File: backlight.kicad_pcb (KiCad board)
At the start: 2 copper layers, 29.3 x 19.6 mm, 18 parts, among them P1 CONN_01X05, U1 APA102C, U2 APA102C, U3 APA102C, U4 APA102C, U5 APA102C, U6 APA102C, U7 APA102C, U8 APA102C, U9 APA102C

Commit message: Modified pcb design
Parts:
- removed the REF** at (148.6, 68.5)
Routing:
- net GND: track 3.06 -> 1.16 mm
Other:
- board size 29.3 x 19.6 mm -> 27.8 x 19.6 mm
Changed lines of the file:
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@@
 (kicad_pcb (version 4) (host pcbnew 4.0.2-stable)
   (general
-    (links 42)
+    (links 41)
     (no_connects 0)
     (area 117.296429 53.075 155.703572 78.675)
     (thickness 1.6)
     (drawings 4)
-    (tracks 100)
+    (tracks 99)
     (zones 0)
-    (modules 18)
+    (modules 17)
     (nets 22)
   )
@@
   )
   (setup
-    (last_trace_width 0.3)
+    (last_trace_width 0.25)
     (user_trace_width 0.3)
     (user_trace_width 0.5)
@@
     (trace_min 0.2)
     (segment_width 0.2)
-    (edge_width 0.15)
+    (edge_width 0.05)
     (via_size 0.6)
     (via_drill 0.4)
@@
     (mod_text_size 1 1)
     (mod_text_width 0.15)
-    (pad_size 1.5 1.5)
-    (pad_drill 1.5)
+    (pad_size 1.3 2)
+    (pad_drill 0)
     (pad_to_mask_clearance 0.2)
     (aux_axis_origin 154 55.6)
@@
     (visible_elements 7FFFFF7F)
     (pcbplotparams
-      (layerselection 0x00000_80000001)
+      (layerselection 0x01008_80000001)
       (usegerberextensions false)
       (excludeedgelayer true)
@@
       (psnegative false)
       (psa4output false)
-      (plotreference true)
-      (plotvalue true)
+      (plotreference false)
+      (plotvalue false)
       (plotinvisibletext false)
       (padsonsilk false)
@@
     (fp_line (start 6.8 4.8) (end 6.8 -4.1) (layer F.CrtYd) (width 0.05))
     (fp_line (start 6.8 -4.1) (end -6.8 -4.1) (layer F.CrtYd) (width 0.05))
-    (pad 1 smd rect (at -2.5 -2.44 90) (size 0.8 1.9) (layers F.Cu F.Paste F.Mask)
+    (pad 1 thru_hole rect (at -2.5 -2.44 90) (size 0.8 1.9) (drill 0.5) (layers *.Cu *.Mask F.SilkS)
       (net 1 GND))
     (pad 2 smd rect (at -1.25 -2.44 90) (size 0.8 1.9) (layers F.Cu F.Paste F.Mask)
@@
     (pad 5 smd rect (at 2.5 -2.44 90) (size 0.8 1.9) (layers F.Cu F.Paste F.Mask)
       (net 20 /MOSI))
-    (pad "" smd rect (at 5.35 2.44 90) (size 1.3 3.35) (layers F.Cu F.Paste F.Mask))
-    (pad "" smd rect (at -5.35 2.44 90) (size 1.3 3.35) (layers F.Cu F.Paste F.Mask))
+    (pad "" smd rect (at 5.35 1.56 90) (size 1.3 2) (layers F.Cu F.Paste F.Mask))
+    (pad "" smd rect (at -5.35 1.56 90) (size 1.3 2) (layers F.Cu F.Paste F.Mask))
     (model Connectors_Molex.3dshapes/Molex_Panelmate-53780-0570_05x1.25mm_Angled.wrl
       (at (xyz 0 0 0))
@@
       (rotate (xyz 0 0 0))
     )
-  )
-  (module backlight:1pin (layer F.Cu)
-    (at 148.6 68.5)
-    (descr "module 1 pin (ou trou mecanique de percage)")
-    (tags DEV)
-    (fp_text reference REF** (at 0 -3.048) (layer F.SilkS) hide
-      (effects (font (size 1 1) (thickness 0.15)))
-    )
-    (fp_text value 1pin (at 0 2.794) (layer F.Fab) hide
-      (effects (font (size 1 1) (thickness 0.15)))
-    )
-    (pad 1 thru_hole circle (at 0 0) (size 1 1) (drill 0.4) (layers *.Cu *.Mask F.SilkS)
-      (net 1 GND))
   )
   (module backlight:TantalC_SizeR_EIA-2012 (layer F.Cu)
@@
     )
   )
-  (gr_line (start 153.3 75.8) (end 153.3 56.2) (layer Edge.Cuts) (width 0.15))
-  (gr_line (start 124 75.8) (end 153.3 75.8) (layer Edge.Cuts) (width 0.15))
-  (gr_line (start 124 56.2) (end 124 75.8) (layer Edge.Cuts) (width 0.15))
-  (gr_line (start 153.3 56.2) (end 124 56.2) (layer Edge.Cuts) (width 0.15))
+  (gr_line (start 151.8 75.8) (end 151.8 56.2) (layer Edge.Cuts) (width 0.05))
+  (gr_line (start 124 75.8) (end 151.8 75.8) (layer Edge.Cuts) (width 0.05))
+  (gr_line (start 124 56.2) (end 124 75.8) (layer Edge.Cuts) (width 0.05))
+  (gr_line (start 151.8 56.2) (end 124 56.2) (layer Edge.Cuts) (width 0.05))
   (segment (start 146.55 69.6) (end 146.55 68.65) (width 0.5) (layer F.Cu) (net 1))
   (segment (start 146.55 68.65) (end 146.7 68.5) (width 0.5) (layer F.Cu) (net 1))
-  (segment (start 146.7 68.5) (end 148.6 68.5) (width 0.8) (layer F.Cu) (net 1))
   (segment (start 137.6 60.75) (end 139 60.75) (width 1) (layer F.Cu) (net 2))
   (segment (start 137.6 62.25) (end 139 62.25) (width 1) (layer F.Cu) (net 3))

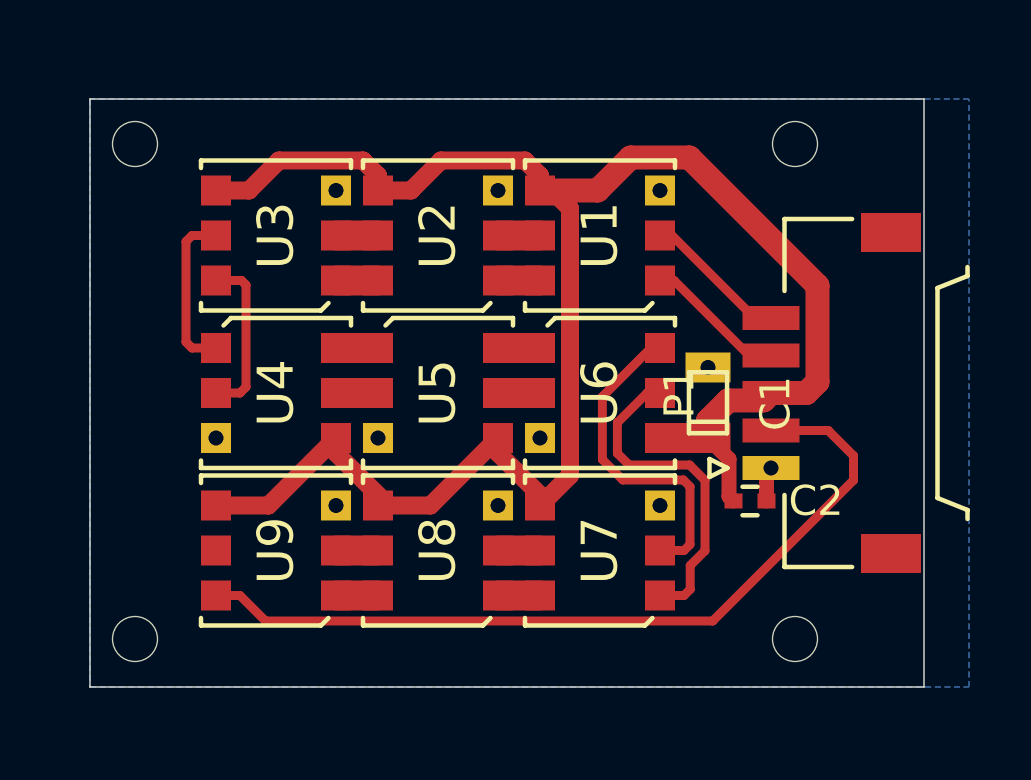
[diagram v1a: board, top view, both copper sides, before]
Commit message: Avoid long staight trace
To make it more auto level friendly
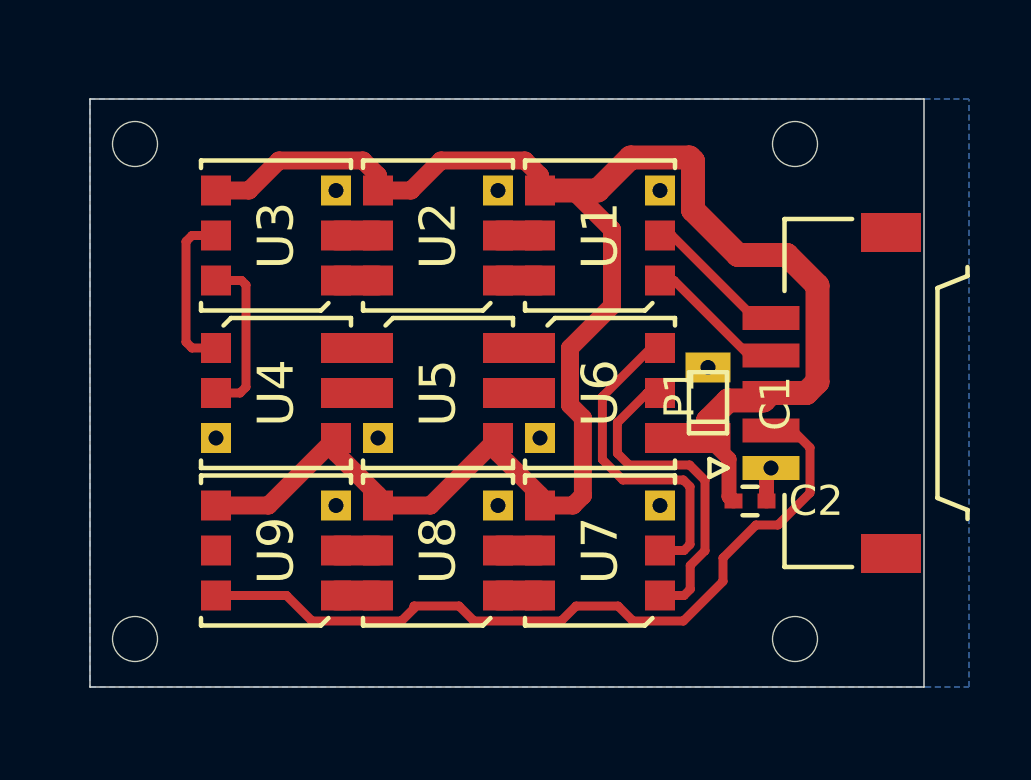
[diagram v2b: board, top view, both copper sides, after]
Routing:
- net VCC: track 63.9 -> 67.8 mm
- net /MISO: track 27.5 -> 26.3 mm
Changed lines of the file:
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@@
     (thickness 1.6)
     (drawings 4)
-    (tracks 99)
+    (tracks 122)
     (zones 0)
     (modules 17)
@@
   )
   (setup
-    (last_trace_width 0.25)
+    (last_trace_width 0.3)
     (user_trace_width 0.3)
     (user_trace_width 0.5)
@@
     (pad_drill 0)
     (pad_to_mask_clearance 0.2)
-    (aux_axis_origin 154 55.6)
-    (grid_origin 154 55.6)
+    (aux_axis_origin 152 55.9)
+    (grid_origin 152 55.9)
     (visible_elements 7FFFFF7F)
     (pcbplotparams
@@
   (segment (start 137.6 71.25) (end 139 71.25) (width 1) (layer F.Cu) (net 12))
   (segment (start 137.6 72.75) (end 139 72.75) (width 1) (layer F.Cu) (net 13))
-  (segment (start 139 69.75) (end 140.000001 68.749999) (width 0.6) (layer F.Cu) (net 14))
-  (segment (start 140.000001 68.749999) (end 140.000001 59.849999) (width 0.6) (layer F.Cu) (net 14))
-  (segment (start 140.000001 59.849999) (end 139.400002 59.25) (width 0.6) (layer F.Cu) (net 14))
+  (segment (start 145.6 61.4) (end 147.230002 61.4) (width 0.8) (layer F.Cu) (net 14))
+  (segment (start 147.230002 61.4) (end 148.250001 62.419999) (width 0.8) (layer F.Cu) (net 14))
+  (segment (start 144.100001 59.900001) (end 145.6 61.4) (width 0.8) (layer F.Cu) (net 14))
+  (segment (start 143.980001 58.149999) (end 144.100001 58.269999) (width 0.8) (layer F.Cu) (net 14))
+  (segment (start 144.100001 58.269999) (end 144.100001 59.900001) (width 0.8) (layer F.Cu) (net 14))
+  (segment (start 140.000001 66.400001) (end 140.42998 66.82998) (width 0.6) (layer F.Cu) (net 14))
+  (segment (start 140.42998 66.82998) (end 140.42998 69.42002) (width 0.6) (layer F.Cu) (net 14))
+  (segment (start 140.42998 69.42002) (end 140.1 69.75) (width 0.6) (layer F.Cu) (net 14))
+  (segment (start 140.1 69.75) (end 139 69.75) (width 0.6) (layer F.Cu) (net 14))
+  (segment (start 141.4 63.1) (end 140.000001 64.499999) (width 0.6) (layer F.Cu) (net 14))
+  (segment (start 140.000001 64.499999) (end 140.000001 66.400001) (width 0.6) (layer F.Cu) (net 14))
+  (segment (start 141.4 60.55) (end 141.4 63.1) (width 0.6) (layer F.Cu) (net 14))
+  (segment (start 139 59.25) (end 140.1 59.25) (width 0.6) (layer F.Cu) (net 14))
+  (segment (start 140.1 59.25) (end 141.4 60.55) (width 0.6) (layer F.Cu) (net 14))
   (segment (start 139.400002 59.25) (end 139 59.25) (width 0.6) (layer F.Cu) (net 14))
   (segment (start 139 59.25) (end 140.919998 59.25) (width 0.8) (layer F.Cu) (net 14))
@@
   (segment (start 142.019999 58.149999) (end 143.980001 58.149999) (width 0.8) (layer F.Cu) (net 14))
   (segment (start 148.250001 65.630001) (end 147.880002 66) (width 0.8) (layer F.Cu) (net 14))
-  (segment (start 143.980001 58.149999) (end 148.250001 62.419999) (width 0.8) (layer F.Cu) (net 14))
   (segment (start 148.250001 62.419999) (end 148.250001 65.630001) (width 0.8) (layer F.Cu) (net 14))
   (segment (start 147.880002 66) (end 146.7 66) (width 0.8) (layer F.Cu) (net 14))
@@
   (segment (start 132.2 71.25) (end 133.6 71.25) (width 1) (layer F.Cu) (net 17))
   (segment (start 132.2 72.75) (end 133.6 72.75) (width 1) (layer F.Cu) (net 18))
-  (segment (start 146.7 67.25) (end 148.608002 67.25) (width 0.3) (layer F.Cu) (net 19))
-  (segment (start 148.608002 67.25) (end 149.450001 68.091999) (width 0.3) (layer F.Cu) (net 19))
-  (segment (start 149.450001 68.091999) (end 149.450001 68.908001) (width 0.3) (layer F.Cu) (net 19))
-  (segment (start 149.450001 68.908001) (end 144.758001 73.600001) (width 0.3) (layer F.Cu) (net 19))
-  (segment (start 144.758001 73.600001) (end 129.850001 73.600001) (width 0.3) (layer F.Cu) (net 19))
-  (segment (start 129.850001 73.600001) (end 129 72.75) (width 0.3) (layer F.Cu) (net 19))
-  (segment (start 129 72.75) (end 128.2 72.75) (width 0.3) (layer F.Cu) (net 19))
+  (segment (start 145.1 71.5) (end 145.1 72.280002) (width 0.3) (layer F.Cu) (net 19))
+  (segment (start 145.1 72.280002) (end 143.780002 73.6) (width 0.3) (layer F.Cu) (net 19))
+  (segment (start 146.2 70.4) (end 145.1 71.5) (width 0.3) (layer F.Cu) (net 19))
+  (segment (start 146.930002 70.4) (end 146.2 70.4) (width 0.3) (layer F.Cu) (net 19))
+  (segment (start 148.000001 69.330001) (end 146.930002 70.4) (width 0.3) (layer F.Cu) (net 19))
+  (segment (start 131.400001 73.600001) (end 130.55 72.75) (width 0.3) (layer F.Cu) (net 19))
+  (segment (start 130.55 72.75) (end 128.2 72.75) (width 0.3) (layer F.Cu) (net 19))
+  (segment (start 134.8 73.1) (end 134.8 73.180002) (width 0.3) (layer F.Cu) (net 19))
+  (segment (start 134.8 73.180002) (end 134.380001 73.600001) (width 0.3) (layer F.Cu) (net 19))
+  (segment (start 134.380001 73.600001) (end 131.400001 73.600001) (width 0.3) (layer F.Cu) (net 19))
+  (segment (start 136.3 73.1) (end 134.8 73.1) (width 0.3) (layer F.Cu) (net 19))
+  (segment (start 136.80001 73.60001) (end 136.3 73.1) (width 0.3) (layer F.Cu) (net 19))
+  (segment (start 140.202085 73.102085) (end 139.70416 73.60001) (width 0.3) (layer F.Cu) (net 19))
+  (segment (start 139.70416 73.60001) (end 136.80001 73.60001) (width 0.3) (layer F.Cu) (net 19))
+  (segment (start 142.1 73.6) (end 141.602085 73.102085) (width 0.3) (layer F.Cu) (net 19))
+  (segment (start 141.602085 73.102085) (end 140.202085 73.102085) (width 0.3) (layer F.Cu) (net 19))
+  (segment (start 143.780002 73.6) (end 142.1 73.6) (width 0.3) (layer F.Cu) (net 19))
+  (segment (start 146.7 67.25) (end 147.430002 67.25) (width 0.3) (layer F.Cu) (net 19))
+  (segment (start 147.430002 67.25) (end 148.000001 67.819999) (width 0.3) (layer F.Cu) (net 19))
+  (segment (start 148.000001 67.819999) (end 148.000001 69.330001) (width 0.3) (layer F.Cu) (net 19))
   (segment (start 146.7 63.5) (end 146.15 63.5) (width 0.3) (layer F.Cu) (net 20))
   (segment (start 146.15 63.5) (end 143.4 60.75) (width 0.3) (layer F.Cu) (net 20))

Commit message: Modified pcb design for easy solidering
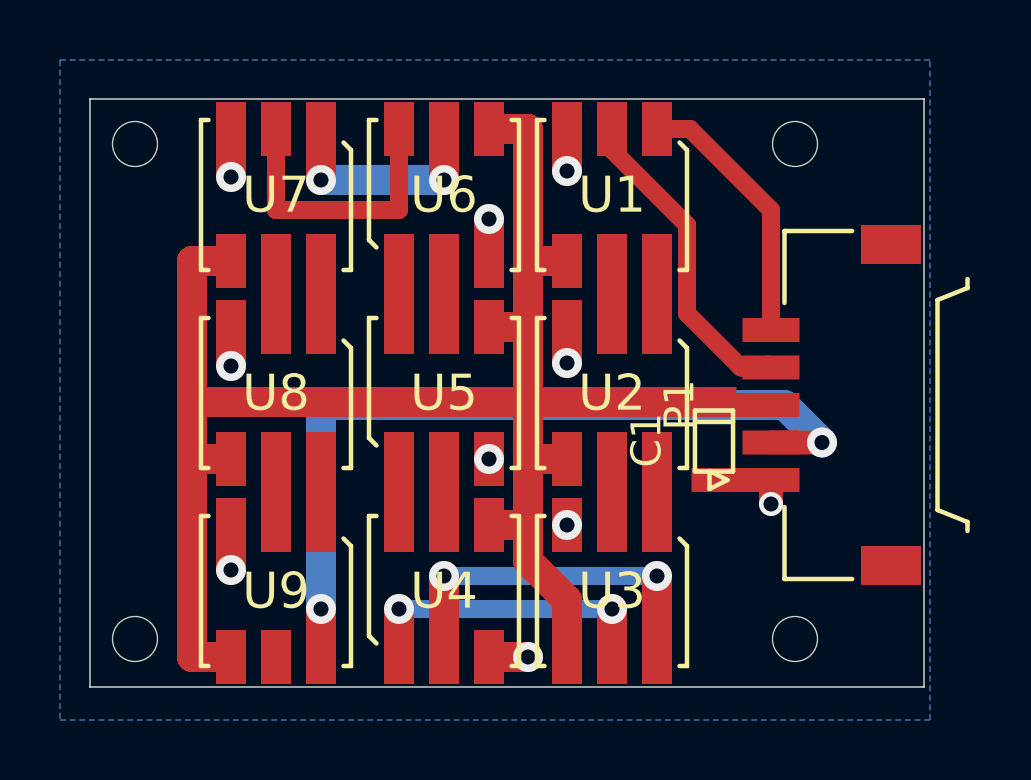
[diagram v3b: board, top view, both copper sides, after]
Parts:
- removed C2: 0.1uF, Capacitors_SMD:C_0402
- moved U3 16.3 mm to (141.4, 72.6), turned to 0 degrees
- moved U7 16.0 mm to (130.2, 59.4), turned to 0 degrees
- moved U4 8.66 mm to (135.8, 72.6), turned to 180 degrees
- moved U6 8.40 mm to (135.8, 59.4), turned to 180 degrees
- moved U2 7.82 mm to (141.4, 66.0), turned to 0 degrees
- moved U8 7.53 mm to (130.2, 66.0), turned to 0 degrees
- moved U1 1.41 mm to (141.4, 59.4), turned to 0 degrees
- moved U9 1.35 mm to (130.2, 72.6), turned to 0 degrees
- moved C1 1.29 mm to (144.8, 67.6), turned to 90 degrees
- moved #P1 0.40 mm to (149.1, 66.4)
- moved P1 0.40 mm to (149.1, 66.4)
- moved U5 0.20 mm to (135.8, 66.0), turned to 180 degrees
- renumbered REF** to #P1
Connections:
- P1 pad 4: /CLK -> /MOSI
- P1 pad 5: /MOSI -> /CLK
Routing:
- net GND: track 1.16 -> 12.6 mm, vias 0 -> 10
- net Net-(U3-Pad6): track 5.54 -> 12.5 mm, vias 0 -> 2
- net VCC: track 67.8 -> 61.3 mm
- net /MOSI: track 4.84 -> 10.9 mm
- net /CLK: track 4.74 -> 9.47 mm
- net Net-(U3-Pad5): track 5.82 -> 10.3 mm, vias 0 -> 2
- net Net-(U6-Pad5): track 11.4 -> 7.50 mm, vias 0 -> 2
- net Net-(U6-Pad6): track 11.0 -> 9.90 mm
- net /MISO: track 26.3 -> 27.3 mm, vias 0 -> 2
- net Net-(U8-Pad6): track 1.40 -> 2.20 mm
- net Net-(U8-Pad5): track 1.40 -> 2.20 mm
- net Net-(U4-Pad6): track 1.40 -> 2.20 mm
- net Net-(U4-Pad5): track 1.40 -> 2.20 mm
- net Net-(U2-Pad6): track 1.40 -> 2.20 mm
- net Net-(U2-Pad5): track 1.40 -> 2.20 mm
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
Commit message: Fixed connection error
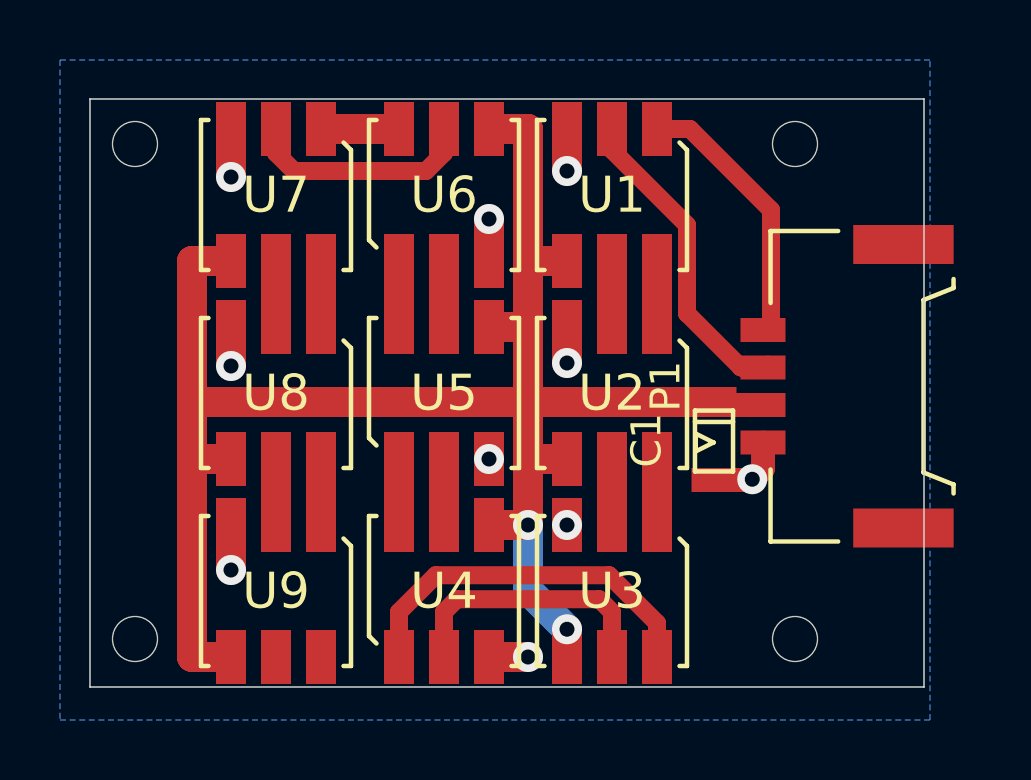
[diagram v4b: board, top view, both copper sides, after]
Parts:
- removed #P1: Molex_Panelmate-51146-0500, Connectors_Molex:Molex_Panelmate-51146-0500
- P1: footprint Connectors_Molex:Molex_Panelmate-53780-0570_05x1.25mm_Angled -> Connectors_Molex:Molex_Panelmate-53780-0470_04x1.25mm_Angled
- moved P1 0.78 mm to (148.7, 65.8)
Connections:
- P1 pad 2: /MISO -> VCC
- P1 pad 3: VCC -> /CLK
- U1 pad 1: /CLK -> /MOSI
- U1 pad 2: /MOSI -> /CLK
- U4 pad 1: Net-(U3-Pad5) -> Net-(U3-Pad6)
- U4 pad 2: Net-(U3-Pad6) -> Net-(U3-Pad5)
- U7 pad 1: Net-(U6-Pad5) -> Net-(U6-Pad6)
- U7 pad 2: Net-(U6-Pad6) -> Net-(U6-Pad5)
- U9 pad 6: /MISO -> (no net)
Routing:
- net /MISO: track 27.3 -> 0.00 mm, vias 2 -> 0
- net Net-(U6-Pad6): track 9.90 -> 3.00 mm
- net /MOSI: track 10.9 -> 9.47 mm
- net /CLK: track 9.47 -> 10.9 mm
- net Net-(U3-Pad5): track 10.3 -> 8.95 mm, vias 2 -> 0
- net Net-(U6-Pad5): track 7.50 -> 7.70 mm, vias 2 -> 0
- net Net-(U3-Pad6): track 12.5 -> 12.4 mm, vias 2 -> 0
- net VCC: vias 0 -> 2
